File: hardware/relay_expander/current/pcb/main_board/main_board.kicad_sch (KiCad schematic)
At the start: 13 parts, among them J1 Conn_01x07_Socket, J16 Conn_01x20_Socket, J2 Conn_01x07_Socket, J3 Screw_Terminal_01x02, SW1 SW_DIP_x03, U1 MCP23017x-x-SO

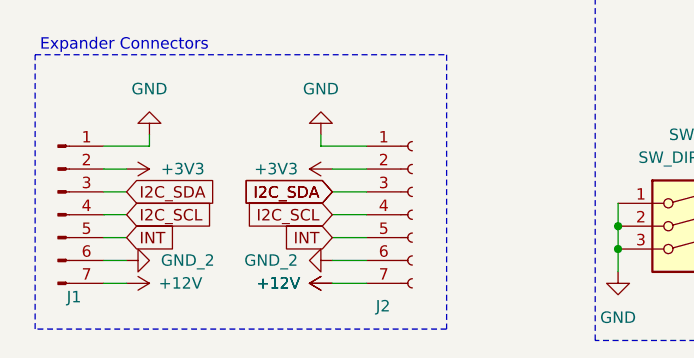
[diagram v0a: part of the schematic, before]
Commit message: [ADD] ui-board for relay - basic layout
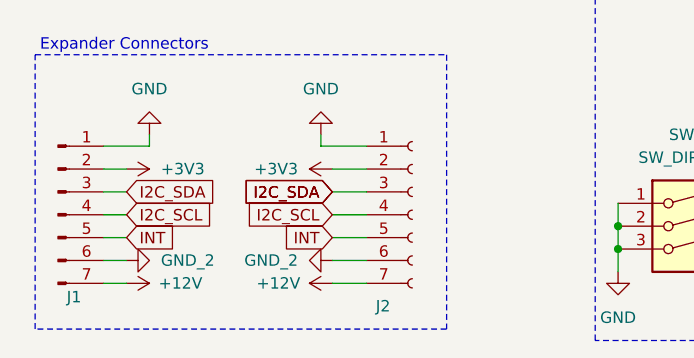
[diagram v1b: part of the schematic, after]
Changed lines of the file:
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@@
 	)
 	(symbol
-		(lib_id "power:+5V")
-		(at 59.69 184.15 90)
+		(lib_id "Device:R_Small")
+		(at 119.38 166.37 0)
 		(unit 1)
 		(body_style 1)
@@
 		(in_pos_files yes)
 		(dnp no)
-		(property "Reference" "#PWR04"
-			(at 63.5 184.15 0)
-			(hide yes)
+		(property "Reference" "R4"
+			(at 116.84 163.83 0)
 			(show_name no)
 			(do_not_autoplace no)
 			(effects
 				(font
-					(size 1.27 1.27)
+					(size 1.016 1.016)
 				)
+				(justify left)
 			)
 		)
-		(property "Value" "+12V"
-			(at 56.134 184.15 90)
+		(property "Value" "10k"
+			(at 120.65 171.45 90)
 			(show_name no)
 			(do_not_autoplace no)
@@
 			)
 		)
-		(property "Footprint" ""
-			(at 59.69 184.15 0)
+		(property "Footprint" "Resistor_SMD:R_1206_3216Metric_Pad1.30x1.75mm_HandSolder"
+			(at 119.38 166.37 0)
 			(hide yes)
 			(show_name no)
@@
 		)
 		(property "Datasheet" ""
-			(at 59.69 184.15 0)
+			(at 119.38 166.37 0)
 			(hide yes)
 			(show_name no)
@@
 			)
 		)
-		(property "Description" "Power symbol creates a global label with name \"+5V\""
-			(at 59.69 184.15 0)
+		(property "Description" "Resistor, small symbol"
+			(at 119.38 166.37 0)
 			(hide yes)
 			(show_name no)
@@
 		(pin "1"
 		)
+		(pin "2"
+		)
 		(instances
 			(project "main_board"
 				(path "/14085887-8f36-46fe-a4da-c907d70eabd5"
-					(reference "#PWR04")
+					(reference "R4")
 					(unit 1)
 				)
@@
 					(unit 1)
 				)
-			)
-		)
-	)
-	(symbol
-		(lib_id "Device:R_Small")
-		(at 119.38 166.37 0)
-		(unit 1)
-		(body_style 1)
-		(exclude_from_sim no)
-		(in_bom yes)
-		(on_board yes)
-		(in_pos_files yes)
-		(dnp no)
-		(property "Reference" "R4"
-			(at 116.84 163.83 0)
-			(show_name no)
-			(do_not_autoplace no)
-			(effects
-				(font
-					(size 1.016 1.016)
-				)
-				(justify left)
-			)
-		)
-		(property "Value" "10k"
-			(at 120.65 171.45 90)
-			(show_name no)
-			(do_not_autoplace no)
-			(effects
-				(font
-					(size 1.27 1.27)
-				)
-				(justify left)
-			)
-		)
-		(property "Footprint" "Resistor_SMD:R_1206_3216Metric_Pad1.30x1.75mm_HandSolder"
-			(at 119.38 166.37 0)
-			(hide yes)
-			(show_name no)
-			(do_not_autoplace no)
-			(effects
-				(font
-					(size 1.27 1.27)
-				)
-			)
-		)
-		(property "Datasheet" ""
-			(at 119.38 166.37 0)
-			(hide yes)
-			(show_name no)
-			(do_not_autoplace no)
-			(effects
-				(font
-					(size 1.27 1.27)
-				)
-			)
-		)
-		(property "Description" "Resistor, small symbol"
-			(at 119.38 166.37 0)
-			(hide yes)
-			(show_name no)
-			(do_not_autoplace no)
-			(effects
-				(font
-					(size 1.27 1.27)
-				)
-			)
-		)
-		(pin "1"
-		)
-		(pin "2"
-		)
-		(instances
-			(project "main_board"
-				(path "/14085887-8f36-46fe-a4da-c907d70eabd5"
-					(reference "R4")
-					(unit 1)
-				)

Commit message: [FIX] add 12V trace for expanders and generate gerber for all relays related boards
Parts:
- added F2: 0.5A, Fuse:Fuse_1206_3216Metric, symbol Device:Fuse_Small
- J3: value Screw_Terminal_01x02 -> Screw_Terminal_01x04
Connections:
- net +12V: now also F2.2; no longer J1.7 (Pin_7), J2.7 (Pin_7)
- new net +12V_BUS: F2.1, J1.7 (Pin_7), J2.7 (Pin_7)
